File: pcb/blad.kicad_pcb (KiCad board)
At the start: 2 copper layers, 228.6 x 76.2 mm, 104 parts, among them J1 HRO_TYPE-C-31-M-12, J2 SWD, Q1 AO3401A, SW1 1U, SW10 1U, SW11 1U, SW12 1U, SW13 1.25U, SW14 1U, SW15 1U, SW16 1U, SW17 1U, SW18 1U, SW19 1U, SW2 1U, SW20 1U, SW21 1U, SW22 1U, SW23 1.75U, SW24 1.75U, SW25 1U, SW26 1U, SW27 1U, SW28 1U, SW29 1U, SW3 1U, SW30 1U, SW31 1U, SW32 1U, SW33 1U, SW34 1.25U, SW35 1.25U, SW36 1U, SW37 1.25U, SW38 2.75U, SW39 2.25U, SW4 1U, SW40 1.25U, SW41 1U, SW42 1.25U, SW5 1U, SW6 1U, SW7 1U, SW8 1U, SW9 1U, U1 SRV05-4, U2 MS88SF21 1Y40AI-U

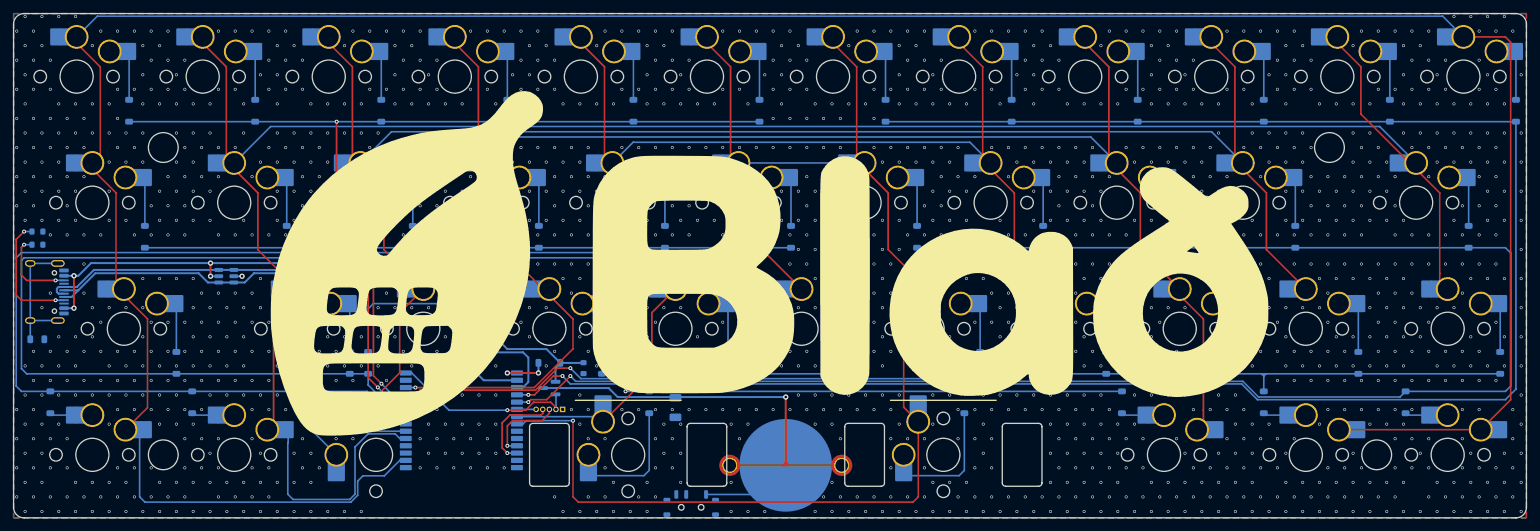
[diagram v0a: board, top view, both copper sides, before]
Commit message: Add mounting holes and update case geometry
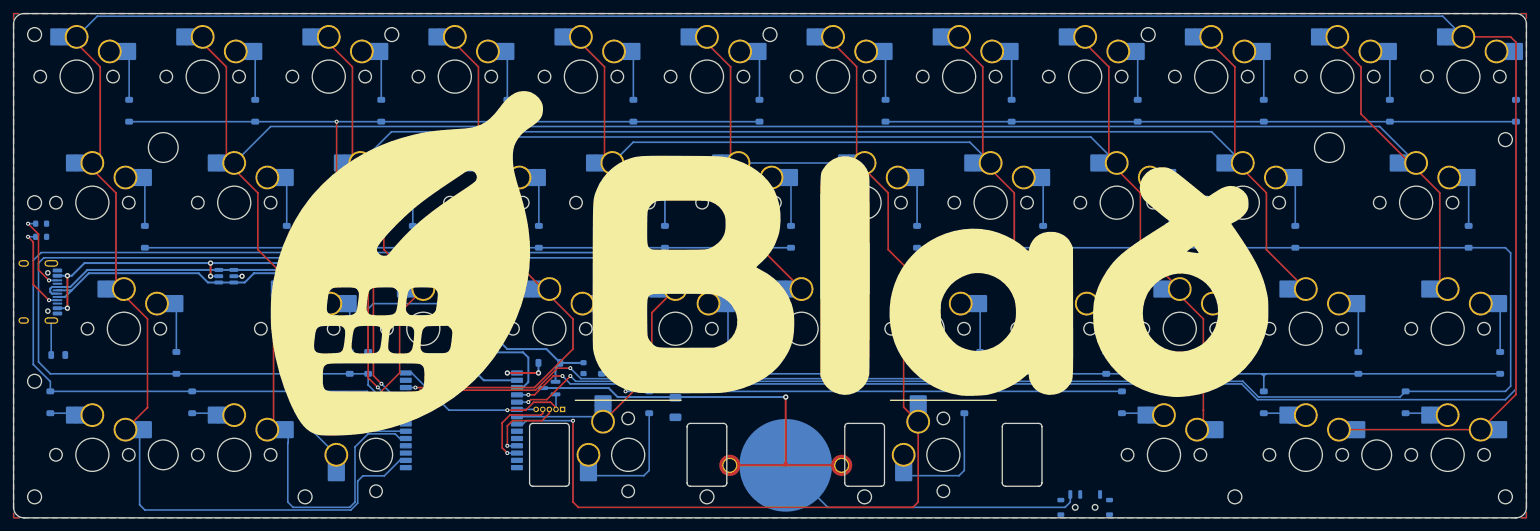
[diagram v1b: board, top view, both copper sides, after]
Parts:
- added H1: MountingHole, MountingHole:MountingHole_2.1mm, F.Cu at (315.1, 128.6)
- added H10: MountingHole, MountingHole:MountingHole_2.1mm, F.Cu at (194.5, 182.6)
- added H11: MountingHole, MountingHole:MountingHole_2.1mm, F.Cu at (218.3, 182.6)
- added H12: MountingHole, MountingHole:MountingHole_2.1mm, F.Cu at (133.7, 182.6)
- added H13: MountingHole, MountingHole:MountingHole_2.1mm, F.Cu at (274.2, 182.6)
- added H2: MountingHole, MountingHole:MountingHole_2.1mm, F.Cu at (315.1, 182.6)
- added H3: MountingHole, MountingHole:MountingHole_2.1mm, F.Cu at (261.1, 112.7)
- added H4: MountingHole, MountingHole:MountingHole_2.1mm, F.Cu at (204.0, 112.7)
- added H5: MountingHole, MountingHole:MountingHole_2.1mm, F.Cu at (146.8, 112.7)
- added H6: MountingHole, MountingHole:MountingHole_2.1mm, F.Cu at (92.9, 112.7)
- added H7: MountingHole, MountingHole:MountingHole_2.1mm, F.Cu at (92.9, 138.1)
- added H8: MountingHole, MountingHole:MountingHole_2.1mm, F.Cu at (92.9, 165.1)
- added H9: MountingHole, MountingHole:MountingHole_2.1mm, F.Cu at (92.9, 182.6)
- moved S1 59.5 mm to (251.6, 184.2)
- moved L2 3.96 mm to (96.4, 161.1)
- moved R3 3.22 mm to (93.9, 141.3)
- moved J1 0.99 mm to (92.3, 151.6)
- moved R1 0.97 mm to (93.9, 143.3)
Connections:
- S1 pad 1: Net-(BT1--) -> unconnected-(S1-A-Pad1)
- S1 pad 3: unconnected-(S1-C-Pad3) -> Net-(BT1--)
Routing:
- net Net-(BT1--): track 13.9 -> 47.1 mm
- net Net-(J1-SHIELD): track 19.8 -> 5.67 mm
- net ROW6: track 269.0 -> 262.6 mm
- net ROW4: track 223.0 -> 217.1 mm
- net Net-(J1-CC1): track 18.8 -> 13.3 mm
- net COL0: track 422.6 -> 426.1 mm
- net COL1: track 332.4 -> 334.8 mm
- net COL5: track 213.9 -> 215.5 mm
- net VBUS: track 76.7 -> 77.7 mm
- net USB_D-: track 78.0 -> 79.0 mm
- net USB_D+: track 77.5 -> 78.5 mm
- net GND: vias 1657 -> 1

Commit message: Refactor application implementation
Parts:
- moved R1 0.20 mm to (94.1, 143.3)
- moved R3 0.20 mm to (94.1, 141.3)

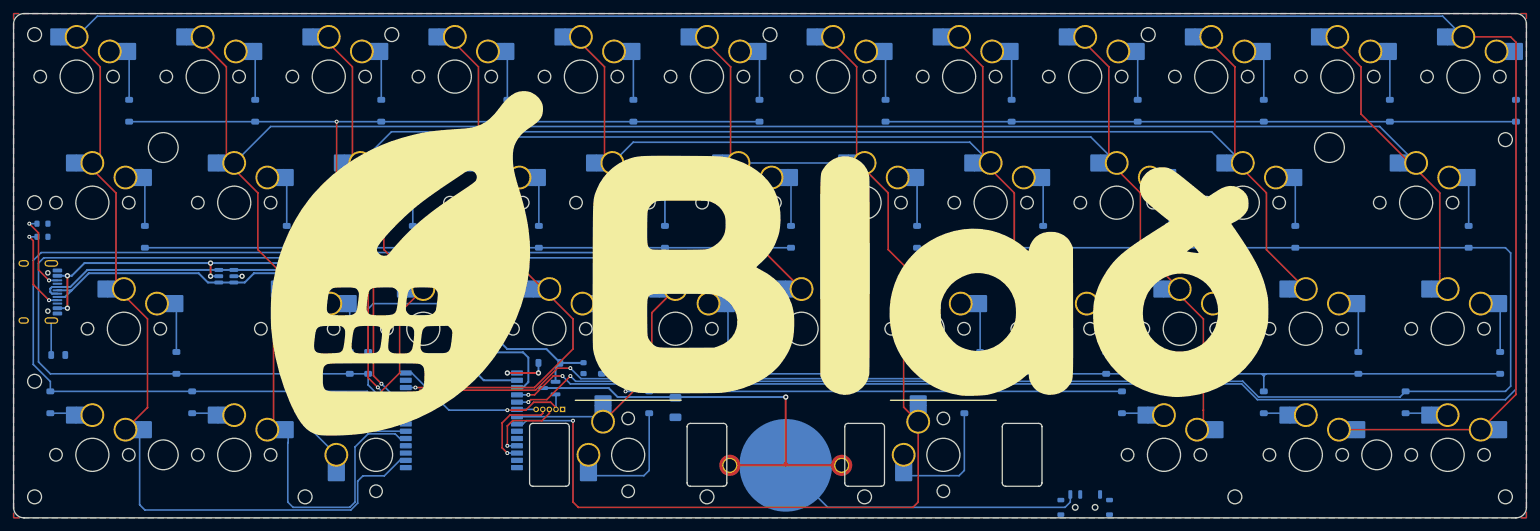
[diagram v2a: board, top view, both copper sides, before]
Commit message: Update PCB routing and schematic connectivity
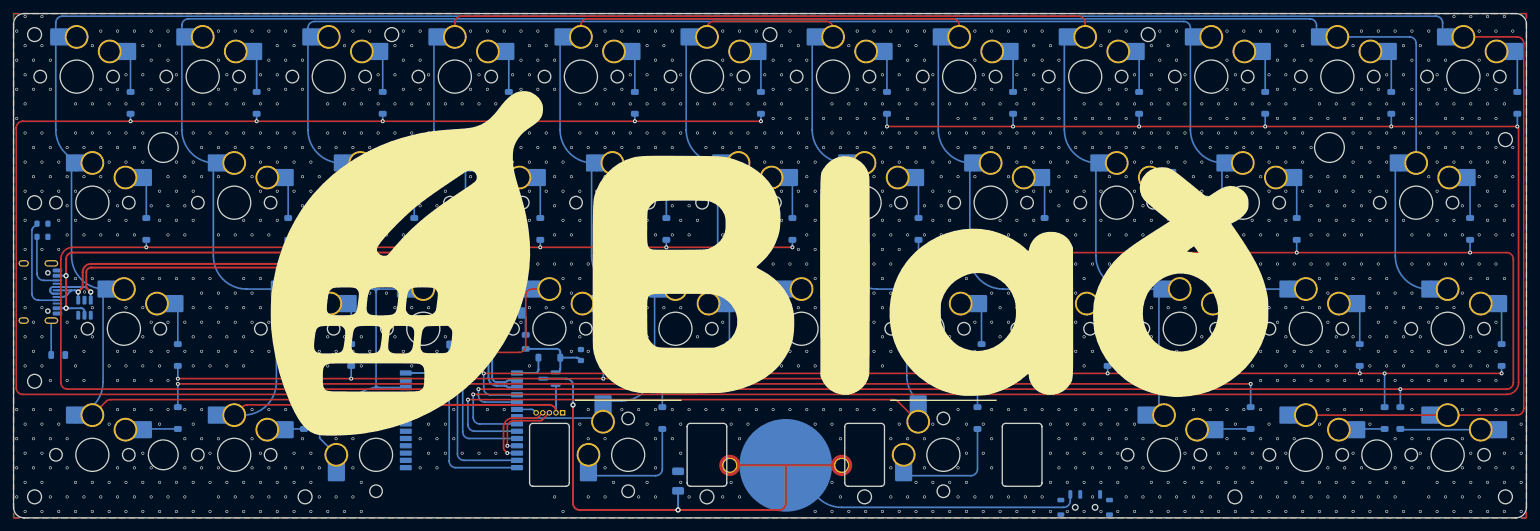
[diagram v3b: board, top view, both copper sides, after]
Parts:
- moved U1 22.0 mm to (100.4, 154.0), turned to -90 degrees
- moved D40 19.6 mm to (276.6, 170.7)
- moved D35 19.4 mm to (114.5, 170.7)
- moved D41 18.4 mm to (296.9, 170.7)
- moved D36 17.1 mm to (133.6, 170.7)
- moved D26 14.2 mm to (157.2, 159.5), turned to 0 degrees
- moved C1 11.1 mm to (190.1, 180.2), turned to 90 degrees
- moved F1 6.16 mm to (165.1, 154.8), turned to 0 degrees
- moved L1 5.95 mm to (167.1, 159.1)
- moved D37 3.24 mm to (135.9, 170.7)
- moved D38 3.10 mm to (187.7, 170.7)
- moved D39 3.10 mm to (235.3, 170.7)
- moved R4 2.58 mm to (162.5, 159.1)
- moved D42 2.51 mm to (299.2, 170.7)
- moved R2 2.02 mm to (175.4, 161.1), turned to -90 degrees
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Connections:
- net Net-(U2-USB_D+) renamed /DP
- net Net-(U2-USB_D-) renamed /DN
- SW35 pad 1: COL0 -> Net-(D35-A)
- SW35 pad 2: Net-(D35-A) -> COL0
- SW36 pad 1: COL1 -> Net-(D36-A)
- SW36 pad 2: Net-(D36-A) -> COL1
- SW40 pad 1: COL3 -> Net-(D40-A)
- SW40 pad 2: Net-(D40-A) -> COL3
- SW41 pad 1: COL0 -> Net-(D41-A)
- SW41 pad 2: Net-(D41-A) -> COL0
- SW42 pad 1: COL0 -> Net-(D42-A)
- SW42 pad 2: Net-(D42-A) -> COL0
- U1 pad 1: USB_D+ -> USB_D-
- U1 pad 3: USB_D- -> USB_D+
- U1 pad 4: USB_D- -> USB_D+
- U1 pad 6: USB_D+ -> USB_D-
- U2 pad 10: ROW2 -> ROW0
- U2 pad 11: ROW5 -> ROW2
- U2 pad 12: COL3 -> COL2
- U2 pad 18: ROW1 -> ROW5
- U2 pad 2: COL0 -> unconnected-(U2-P1.13-Pad2)
- U2 pad 22: COL5 -> ROW1
- U2 pad 23: unconnected-(U2-P0.24-Pad23) -> COL5
- U2 pad 24: unconnected-(U2-P1.00-Pad24) -> ROW6
- U2 pad 27: unconnected-(U2-P0.09-Pad27) -> COL3
- U2 pad 28: unconnected-(U2-P0.10-Pad28) -> ROW4
- U2 pad 5: COL1 -> unconnected-(U2-P0.29-Pad5)
- U2 pad 6: COL2 -> unconnected-(U2-P0.31-Pad6)
- U2 pad 7: ROW6 -> unconnected-(U2-P0.26-Pad7)
- U2 pad 8: ROW4 -> COL1
- U2 pad 9: ROW0 -> COL0
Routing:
- net ROW0: track 143.6 -> 225.3 mm, vias 2 -> 7
- net ROW4: track 217.1 -> 140.4 mm, vias 0 -> 6
- net ROW2: track 123.5 -> 197.9 mm, vias 2 -> 7
- net ROW6: track 262.6 -> 199.1 mm, vias 2 -> 7
- net COL3: track 248.4 -> 278.6 mm
- net ROW1: track 289.9 -> 315.1 mm, vias 2 -> 7
- net COL4: track 185.3 -> 208.5 mm
- net ROW3: track 263.9 -> 285.6 mm, vias 2 -> 7
- net COL5: track 215.5 -> 232.4 mm
- net +BATT: track 65.7 -> 81.6 mm, vias 1 -> 2
- net Net-(D26-A): track 20.2 -> 6.52 mm
- net COL1: track 334.8 -> 348.3 mm, vias 0 -> 1
- net COL2: track 258.4 -> 271.9 mm
- net COL0: track 426.1 -> 438.9 mm, vias 0 -> 1
- net VBUS: track 77.7 -> 88.9 mm, vias 4 -> 3
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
